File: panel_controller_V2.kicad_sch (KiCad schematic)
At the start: 14 parts, among them J1 Screw_Terminal_01x02, J2 Screw_Terminal_01x04, J3 SSW-104-01-F-S, J4 SSW-108-02-G-D, J5 Screw_Terminal_01x03, U1 ESP32-DEVKIT-V1, U2 RA-02_LORA

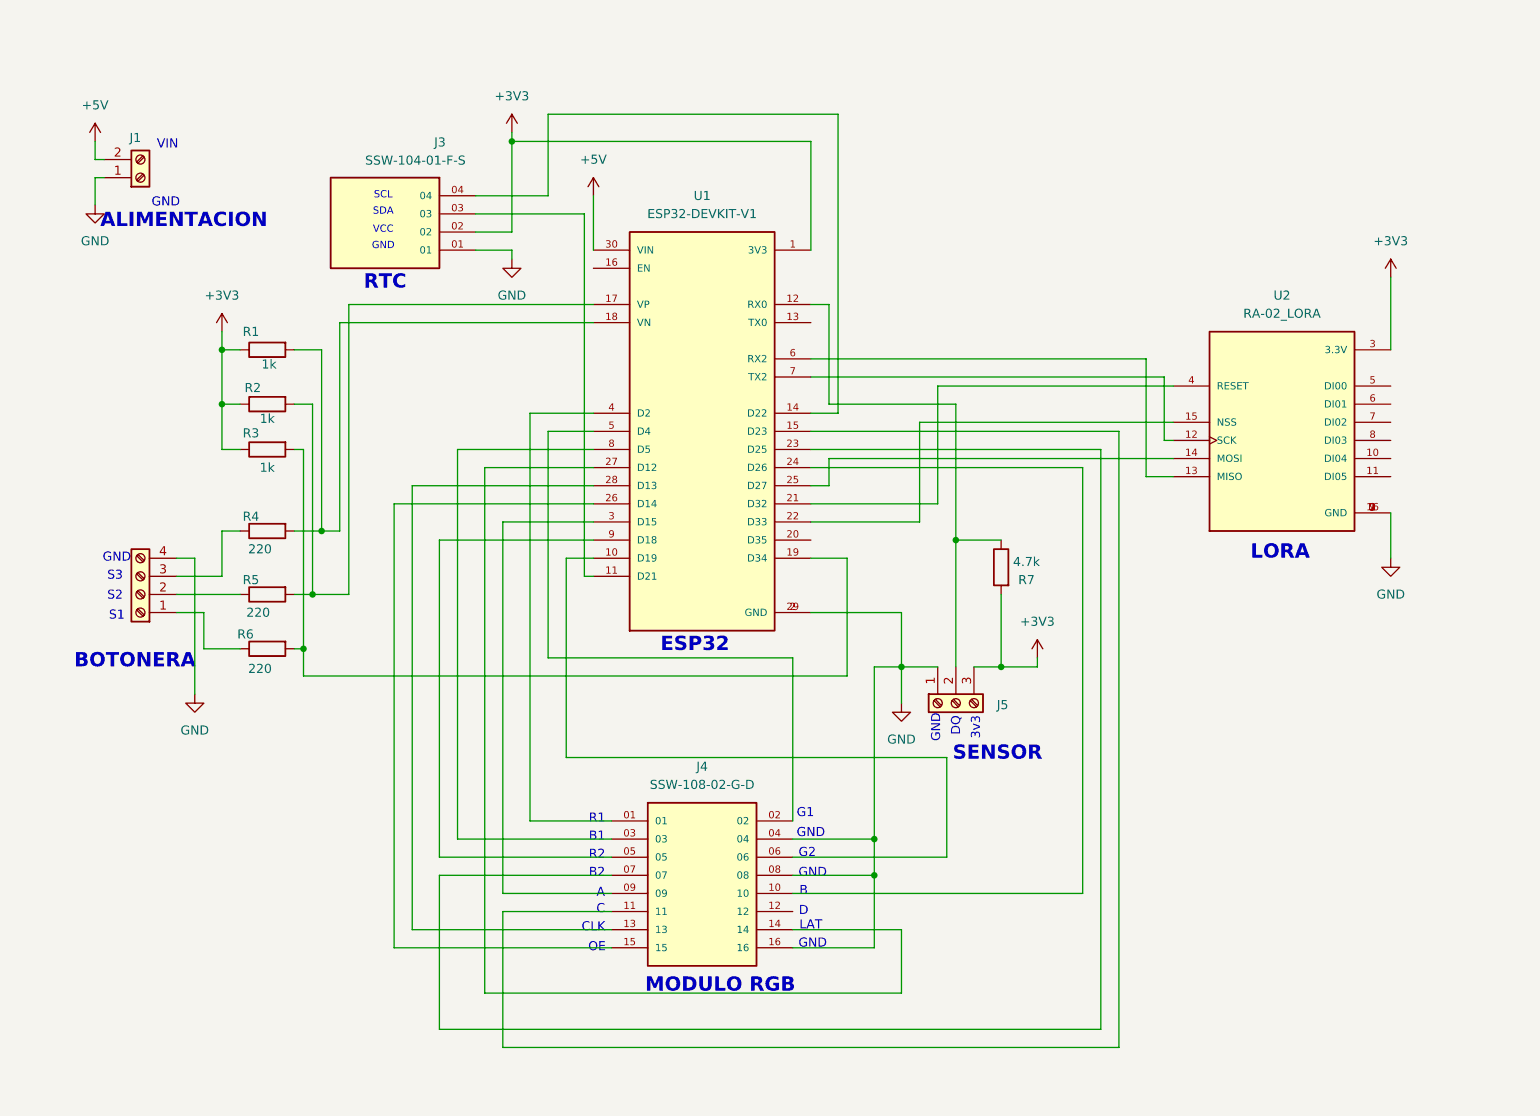
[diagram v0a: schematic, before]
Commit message: headers parallel to esp32 added
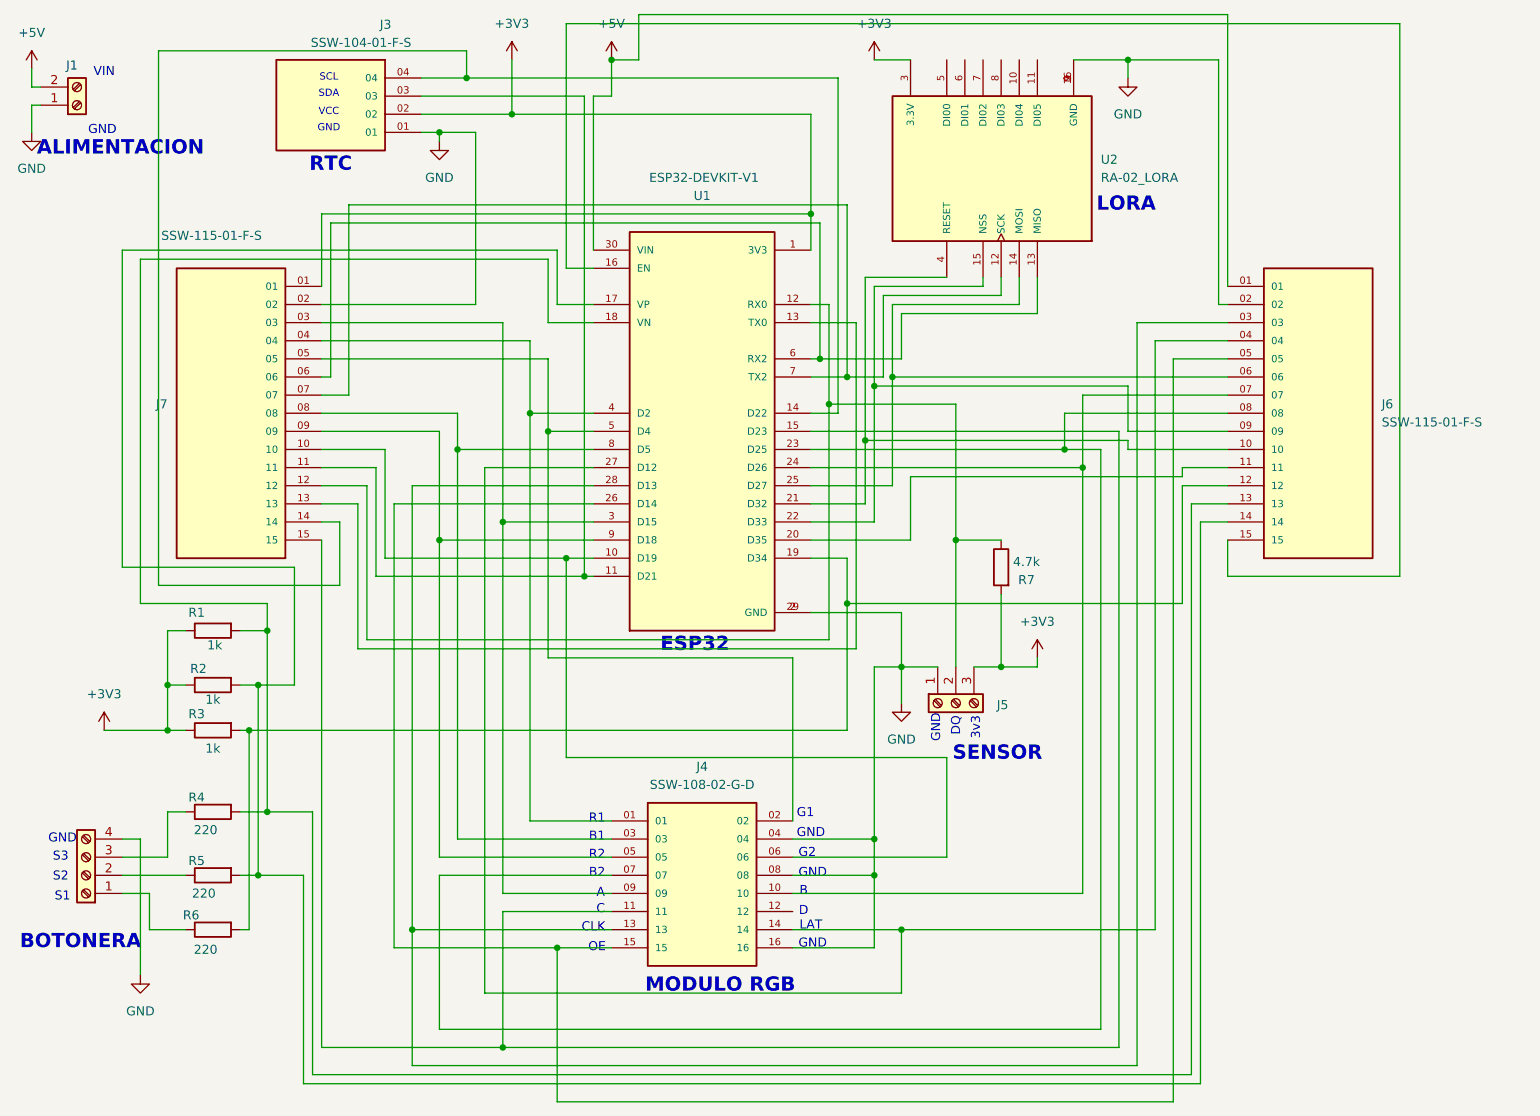
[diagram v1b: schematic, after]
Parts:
- added J6, J7: SSW-115-01-F-S, SSW_115_01_F_S:SAMTEC_SSW-115-01-F-S, symbol SSW-115-01-F-S:SSW-115-01-F-S
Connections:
- net +3V3: now also J7.01
- net +5V: now also J6.01
- net GND: now also J6.02, J7.02
- net at R2.2, R5.2, U1.17 (VP): now also J6.14
- net at J4.01, U1.4 (D2): now also J7.04
- net at J4.02, U1.5 (D4): now also J7.05
- net at J4.03, U1.8 (D5): now also J7.08
- net at J4.05, U1.9 (D18): now also J7.09
- net at J4.06, U1.10 (D19): now also J7.10
- net at J4.07, U1.23 (D25): now also J6.08
- net at J4.09, U1.3 (D15): now also J7.03
- net at J4.10, U1.24 (D26): now also J6.07
- net at J4.11, U1.15 (D23): now also J7.15
- net at J4.13, U1.28 (D13): now also J6.03
- net at J4.14, U1.27 (D12): now also J6.04
- net at J4.15, U1.26 (D14): now also J6.05
- net at J3.03, U1.11 (D21): now also J7.11
- net at J5.2 (Pin_2), R7.1, U1.12 (RX0): now also J7.12
- net at U1.13 (TX0): now also J7.13
- net at J3.04, U1.14 (D22): now also J7.14
- net at U1.16 (EN): now also J6.15
- net at R1.2, R4.2, U1.18 (VN): now also J6.13
- net at R3.2, R6.2, U1.19 (D34): now also J6.12
- net at U1.20 (D35): now also J6.11
- net at U1.21 (D32), U2.4 (RESET): now also J6.10
- net at U1.22 (D33), U2.15 (NSS): now also J6.09
- net at U1.25 (D27), U2.14 (MOSI): now also J6.06
- net at U1.6 (RX2), U2.13 (MISO): now also J7.06
- net at U1.7 (TX2), U2.12 (SCK): now also J7.07
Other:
- moved on the sheet: J1, J3, R1, R2, R3, R4, R5, R6, U2
